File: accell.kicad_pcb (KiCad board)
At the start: 2 copper layers, 9 x 16.1 mm, 6 parts, among them J4 Conn_01x06, U6 LIS3DH

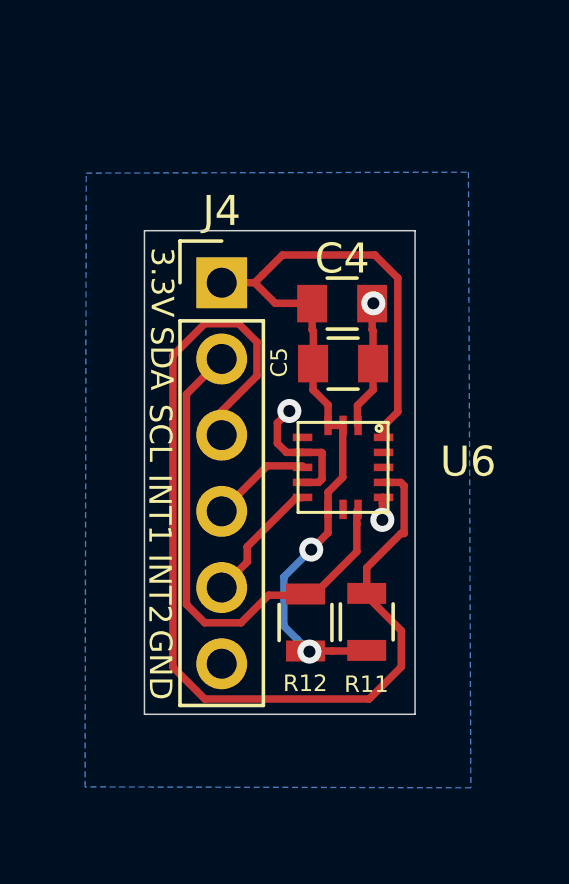
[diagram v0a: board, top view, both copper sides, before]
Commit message: New Power_Management from Pin64 schematic.  Much less parts
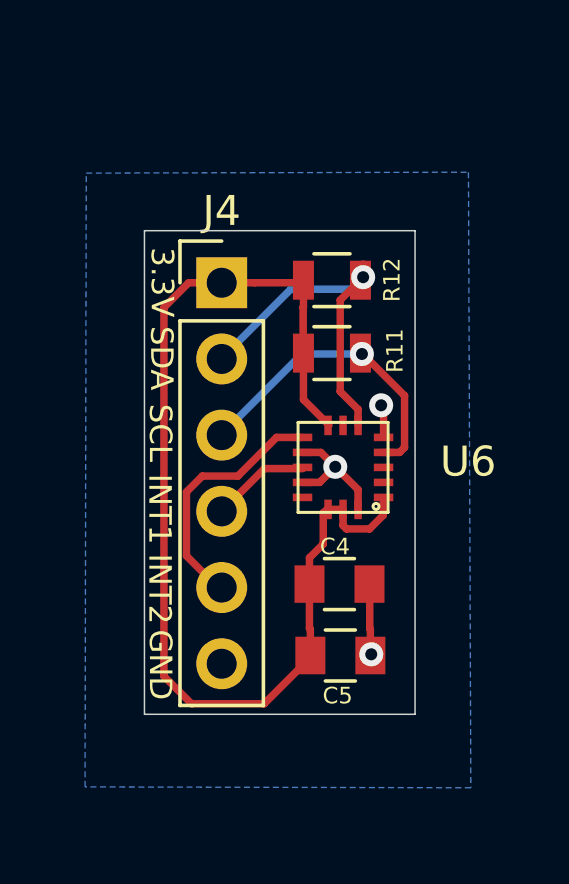
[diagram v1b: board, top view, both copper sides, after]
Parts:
- moved R12 11.4 mm to (129.1, 87.0), turned to 0 degrees
- moved C5 9.73 mm to (129.4, 99.5)
- moved C4 9.35 mm to (129.4, 97.1)
- moved R11 9.03 mm to (129.1, 89.4), turned to 0 degrees
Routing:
- net I2C_SCL: track 33.8 -> 10.3 mm, vias 0 -> 1
- net +3.3: track 29.6 -> 37.7 mm, vias 2 -> 0
- net I2C_SDA: track 16.9 -> 11.8 mm, vias 0 -> 1
- net XL_INT_2: track 4.22 -> 8.34 mm
- net (GND): track 9.44 -> 7.83 mm

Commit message: Initial
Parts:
- removed U6: LIS3DH, my-fp-library:LGA-16_3x3mm
- added IC1: BMA423, SamacSys_Parts:BMA423, F.Cu at (129.6, 96.4)
- C5: value 10uF -> 100nF
- moved C4 10.4 mm to (129.6, 86.8)
- moved C5 6.67 mm to (129.6, 92.8)
- moved R12 1.78 mm to (129.4, 88.7), turned to 180 degrees
- moved R11 1.43 mm to (129.4, 90.8), turned to 180 degrees
- moved J4 0.11 mm to (125.6, 87.1)
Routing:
- net I2C_SCL: track 10.3 -> 28.2 mm, vias 1 -> 0
- net +3.3: track 37.7 -> 22.3 mm, vias 0 -> 2
- net XL_INT_2: track 8.34 -> 3.44 mm
- net (GND): track 7.83 -> 12.0 mm, vias 3 -> 2
- net I2C_SDA: track 11.8 -> 11.1 mm, vias 1 -> 2

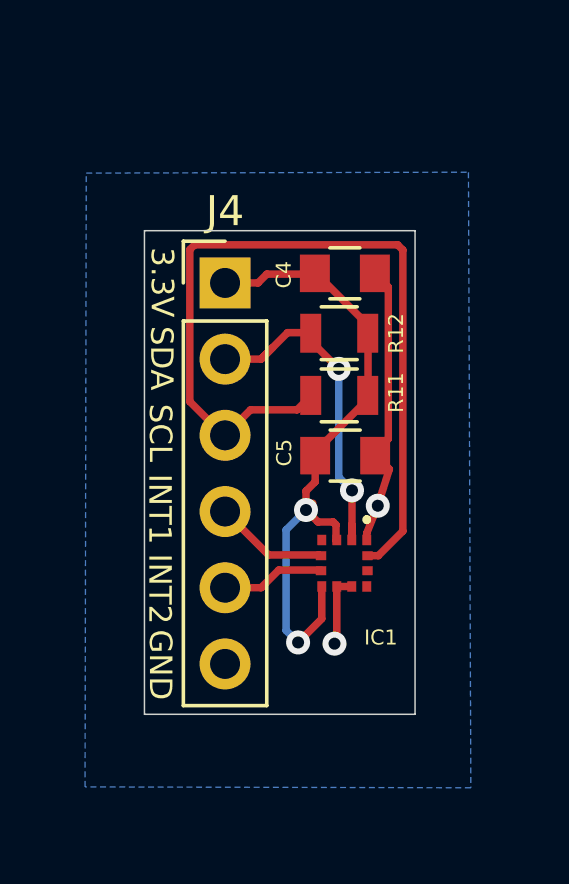
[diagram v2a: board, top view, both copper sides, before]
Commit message: Update footprints
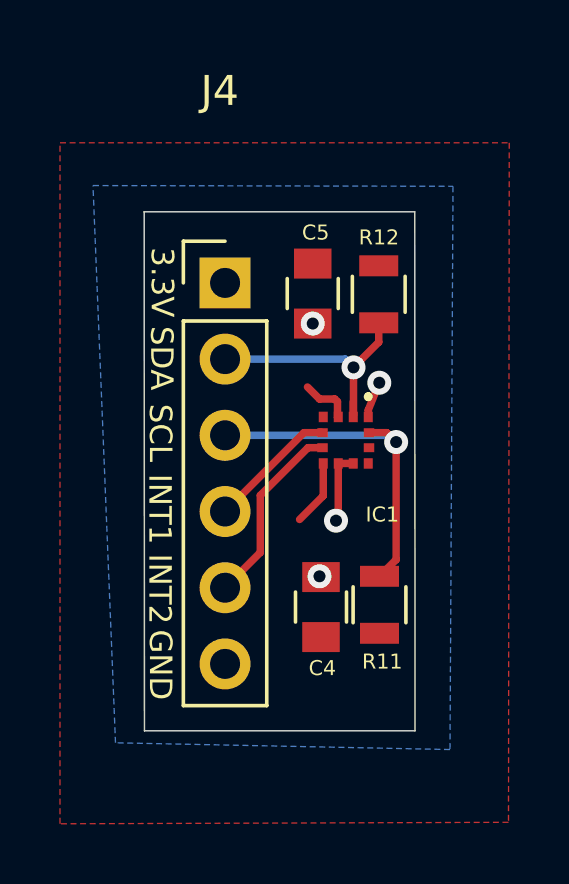
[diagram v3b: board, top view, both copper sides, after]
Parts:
- moved C4 11.2 mm to (128.8, 97.9), turned to 90 degrees
- moved R11 7.11 mm to (130.7, 97.8), turned to 90 degrees
- moved C5 5.51 mm to (128.5, 87.4), turned to 270 degrees
- moved IC1 4.10 mm to (129.6, 92.3)
- moved R12 1.85 mm to (130.7, 87.5), turned to 270 degrees
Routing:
- net +3.3: track 22.3 -> 3.93 mm, vias 2 -> 0
- net I2C_SCL: track 28.2 -> 11.5 mm, vias 0 -> 1
- net (GND): track 12.0 -> 3.65 mm, vias 2 -> 4
- net XL_INT_2: track 3.44 -> 6.30 mm
- net I2C_SDA: track 11.1 -> 8.93 mm, vias 2 -> 1
- net XL_INT_1: track 3.75 -> 4.34 mm
- added copper zone on F.Cu, net +3.3
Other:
- board size 9 x 16.1 mm -> 9 x 17.3 mm
